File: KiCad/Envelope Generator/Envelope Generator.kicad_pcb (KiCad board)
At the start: 2 copper layers, 78 x 57 mm, 64 parts, among them J1 Screw_Terminal_01x03, J2 Screw_Terminal_01x03, U1 TL074, U2 TL074, U3 TL074

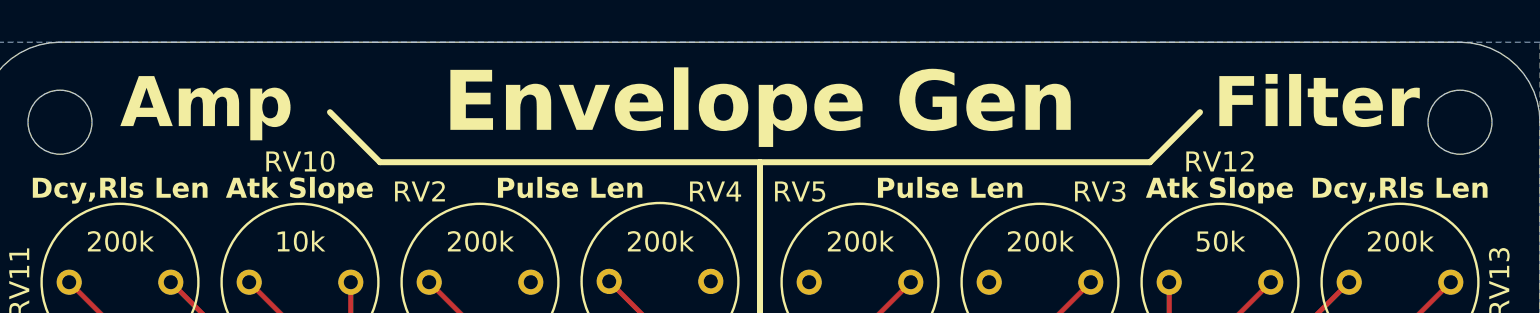
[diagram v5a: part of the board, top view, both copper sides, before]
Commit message: added graphics to some boards
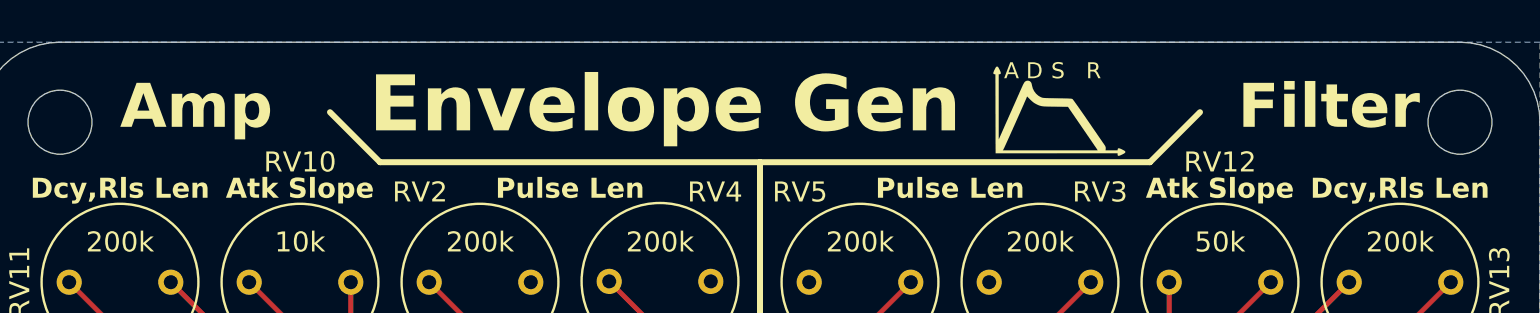
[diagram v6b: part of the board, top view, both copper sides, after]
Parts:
- added G***: LOGO, LOGO, F.Cu at (74.2, 67.3)
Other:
- board text added: "A"
- board text added: "D"
- board text added: "R"
- board text added: "S"
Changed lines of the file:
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@@
 		)
+	)
+	(footprint "LOGO"
+		(layer "F.Cu")
+		(at 74.18424 67.314855)
+		(property "Reference" "G***"
+			(at 0 0 0)
+			(layer "F.SilkS")
+			(hide yes)
+			(effects
+				(font
+					(size 1.5 1.5)
+					(thickness 0.3)
+				)
+			)
+		)
+		(property "Value" "LOGO"
+			(at 0.75 0 0)
+			(layer "F.SilkS")
+			(hide yes)
+			(effects
+				(font
+					(size 1.5 1.5)
+					(thickness 0.3)
+				)
+			)
+		)
+		(property "Datasheet" ""
+			(at 0 0 0)
+			(layer "F.Fab")
+			(hide yes)
+			(effects
+				(font
+					(size 1.27 1.27)
+				)
+			)
+		)
+		(property "Description" ""
+			(at 0 0 0)
+			(layer "F.Fab")
+			(hide yes)
+			(effects
+				(font
+					(size 1.27 1.27)
+				)
+			)
+		)
+		(attr board_only exclude_from_pos_files exclude_from_bom)
+		(duplicate_pad_numbers_are_jumpers no)
+		(fp_poly
+			(pts
+				(xy -9.306532 -4.093194) (xy -9.283506 -4.074777) (xy -9.257123 -4.03656) (xy -9.222403 -3.97239)
+				(xy -9.210337 -3.948591) (xy -9.167452 -3.856319) (xy -9.145899 -3.790321) (xy -9.145474 -3.746886)
+				(xy -9.165972 -3.722302) (xy -9.197348 -3.713709) (xy -9.248111 -3.707868) (xy -9.247606 -2.080061)
+				(xy -9.247101 -0.452253) (xy -8.784721 -1.495204) (xy -8.696641 -1.693897) (xy -8.608126 -1.893602)
+				(xy -8.521165 -2.089834) (xy -8.437744 -2.278106) (xy -8.359851 -2.453933) (xy -8.289474 -2.612828)
+				(xy -8.228598 -2.750307) (xy -8.179213 -2.861883) (xy -8.150939 -2.9258) (xy -8.093309 -3.05493)
+				(xy -8.047459 -3.154353) (xy -8.011013 -3.228461) (xy -7.981598 -3.281645) (xy -7.956838 -3.318295)
+				(xy -7.934361 -3.342804) (xy -7.918871 -3.354979) (xy -7.838689 -3.390617) (xy -7.757425 -3.390332)
+				(xy -7.69886 -3.366673) (xy -7.651872 -3.33137) (xy -7.619915 -3.285472) (xy -7.597977 -3.219446)
+				(xy -7.584937 -3.150051) (xy -7.544939 -3.002166) (xy -7.475037 -2.863153) (xy -7.380375 -2.739656)
+				(xy -7.266095 -2.63832) (xy -7.137341 -2.56579) (xy -7.130544 -2.56301) (xy -7.102187 -2.552074)
+				(xy -7.074249 -2.543107) (xy -7.042758 -2.535853) (xy -7.003739 -2.530059) (xy -6.953218 -2.52547)
+				(xy -6.887223 -2.521832) (xy -6.80178 -2.51889) (xy -6.692916 -2.51639) (xy -6.556656 -2.514078)
+				(xy -6.389027 -2.511699) (xy -6.313082 -2.510682) (xy -6.126615 -2.507997) (xy -5.973666 -2.505262)
+				(xy -5.850836 -2.502309) (xy -5.754725 -2.498972) (xy -5.681933 -2.495082) (xy -5.62906 -2.490472)
+				(xy -5.592706 -2.484974) (xy -5.569472 -2.478421) (xy -5.559842 -2.473547) (xy -5.542448 -2.45397)
+				(xy -5.506066 -2.406431) (xy -5.452499 -2.333477) (xy -5.383549 -2.237653) (xy -5.301022 -2.121506)
+				(xy -5.206718 -1.987581) (xy -5.102444 -1.838424) (xy -4.99 -1.676581) (xy -4.871192 -1.504598)
+				(xy -4.794909 -1.393678) (xy -4.671185 -1.213498) (xy -4.551526 -1.039297) (xy -4.437906 -0.873944)
+				(xy -4.332296 -0.720308) (xy -4.236671 -0.581256) (xy -4.153002 -0.459657) (xy -4.083262 -0.35838)
+				(xy -4.029425 -0.280292) (xy -3.993463 -0.228263) (xy -3.982359 -0.212282) (xy -3.937748 -0.146207)
+				(xy -3.911401 -0.098855) (xy -3.899191 -0.059594) (xy -3.896991 -0.017793) (xy -3.898164 0.004626)
+				(xy -3.904143 0.092319) (xy -3.605406 0.092307) (xy -3.306668 0.092296) (xy -3.300827 0.041533)
+				(xy -3.288668 0.004423) (xy -3.260631 -0.01193) (xy -3.213003 -0.007319) (xy -3.142075 0.018461)
+				(xy -3.065945 0.054522) (xy -2.993287 0.092516) (xy -2.948328 0.120759) (xy -2.924915 0.144232)
+				(xy -2.916896 0.167912) (xy -2.91657 0.175363) (xy -2.921393 0.200174) (xy -2.93999 0.223315) (xy -2.978557 0.249822)
+				(xy -3.043287 0.284736) (xy -3.063835 0.295142) (xy -3.155576 0.338498) (xy -3.221153 0.362466)
+				(xy -3.265039 0.368256) (xy -3.291707 0.35708) (xy -3.29191 0.356879) (xy -3.300898 0.331084) (xy -3.304216 0.291854)
+				(xy -3.304216 0.239134) (xy -6.354615 0.240409) (xy -9.405015 0.241684) (xy -9.40537 0.092296) (xy -9.046164 0.092296)
+				(xy -6.671778 0.092296) (xy -4.297393 0.092296) (xy -4.331509 0.03892) (xy -4.347572 0.0149) (xy -4.382734 -0.036903)
+				(xy -4.435188 -0.113848) (xy -4.503125 -0.21329) (xy -4.584735 -0.332588) (xy -4.67821 -0.469097)
+				(xy -4.781743 -0.620174) (xy -4.893523 -0.783178) (xy -5.011743 -0.955464) (xy -5.075782 -1.048747)
+				(xy -5.785939 -2.083039) (xy -6.423312 -2.090362) (xy -6.604211 -2.09257) (xy -6.752909 -2.095079)
+				(xy -6.874118 -2.098563) (xy -6.972552 -2.103694) (xy -7.052927 -2.111143) (xy -7.119956 -2.121584)
+				(xy -7.178353 -2.135688) (xy -7.232833 -2.154129) (xy -7.288109 -2.177579) (xy -7.348896 -2.20671)
+				(xy -7.392921 -2.228672) (xy -7.480107 -2.279593) (xy -7.56762 -2.34681) (xy -7.664637 -2.437457)
+				(xy -7.67535 -2.448222) (xy -7.828533 -2.602991) (xy -7.855211 -2.539141) (xy -7.884309 -2.470676)
+				(xy -7.925013 -2.376635) (xy -7.975891 -2.260219) (xy -8.035511 -2.124628) (xy -8.102441 -1.973064)
+				(xy -8.17525 -1.808727) (xy -8.252506 -1.634818) (xy -8.332776 -1.454539) (xy -8.414629 -1.27109)
+				(xy -8.496634 -1.087672) (xy -8.577357 -0.907486) (xy -8.655368 -0.733732) (xy -8.729235 -0.569613)
+				(xy -8.797525 -0.418327) (xy -8.858807 -0.283077) (xy -8.911648 -0.167064) (xy -8.954618 -0.073488)
+				(xy -8.986284 -0.005549) (xy -9.005215 0.03355) (xy -9.009629 0.041533) (xy -9.046164 0.092296)
+				(xy -9.40537 0.092296) (xy -9.409713 -1.7331) (xy -9.414411 -3.707884) (xy -9.465091 -3.713717)
+				(xy -9.502166 -3.725887) (xy -9.51848 -3.75396) (xy -9.513827 -3.801642) (xy -9.488001 -3.872638)
+				(xy -9.452018 -3.948591) (xy -9.414025 -4.02125) (xy -9.385781 -4.066208) (xy -9.362308 -4.089621)
+				(xy -9.338628 -4.09764) (xy -9.331178 -4.097966)
+			)
+			(stroke
+				(width 0)
+				(type solid)
+			)
+			(fill yes)
+			(layer "F.SilkS")
+		)
+		(embedded_fonts no)
 	)
 	(footprint "TestPoint:TestPoint_Keystone_5000-5004_Miniature"
@@
 		(layer "Edge.Cuts")
 	)
+	(gr_text "A"
+		(at 65.2 63.9 0)
+		(layer "F.SilkS")
+		(effects
+			(font
+				(size 0.8 0.8)
+				(thickness 0.125)
+			)
+			(justify left bottom)
+		)
+	)
+	(gr_text "D"
+		(at 66.3 63.9 0)
+		(layer "F.SilkS")
+		(effects
+			(font
+				(size 0.8 0.8)
+				(thickness 0.125)
+			)
+			(justify left bottom)
+		)
+	)
+	(gr_text "S"
+		(at 67.55 63.9 0)
+		(layer "F.SilkS")
+		(effects
+			(font
+				(size 0.8 0.8)
+				(thickness 0.125)
+			)
+			(justify left bottom)
+		)
+	)
+	(gr_text "R"
+		(at 69.3 63.9 0)
+		(layer "F.SilkS")
+		(effects
+			(font
+				(size 0.8 0.8)
+				(thickness 0.125)
+			)
+			(justify left bottom)
+		)
+	)
 	(gr_text "100k"
 		(at 20 92.5 0)
@@
 		(effects
 			(font
-				(size 2.5 2.5)
-				(thickness 0.5)
+				(size 2.2 2.2)
+				(thickness 0.44)
 				(bold yes)
 			)
@@
 		(effects
 			(font
-				(size 2.5 2.5)
-				(thickness 0.5)
+				(size 2.2 2.2)
+				(thickness 0.44)
 				(bold yes)
 			)
@@
 	)
 	(gr_text "Envelope Gen"
-		(at 53 66.75 0)
-		(layer "F.SilkS")
-		(effects
-			(font
-				(size 3 3)
-				(thickness 0.6)
-				(bold yes)
-			)
+		(at 48.25 66.75 0)
+		(layer "F.SilkS")
+		(effects
+			(font
+				(size 2.8 2.8)
+				(thickness 0.56)
+				(bold yes)
+			)
